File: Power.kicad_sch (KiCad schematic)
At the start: 10 parts

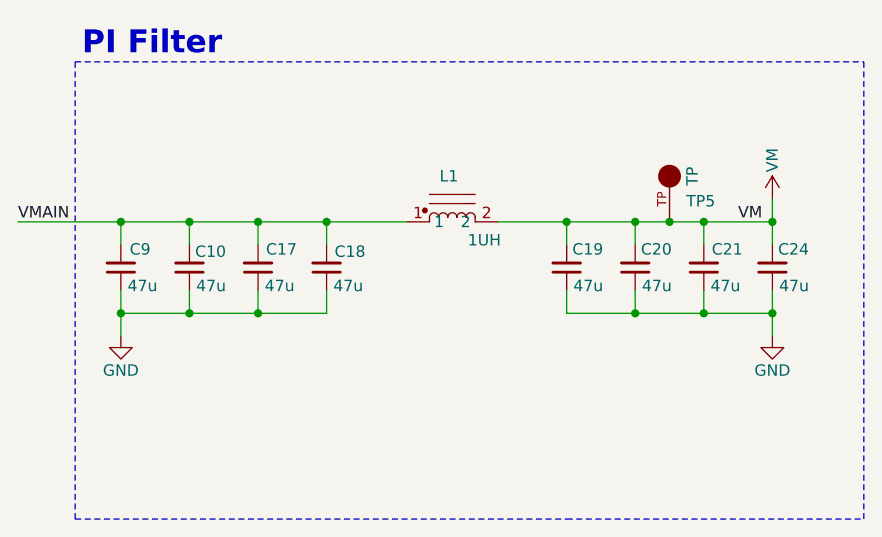
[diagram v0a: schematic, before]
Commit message: moved inductor and added leds
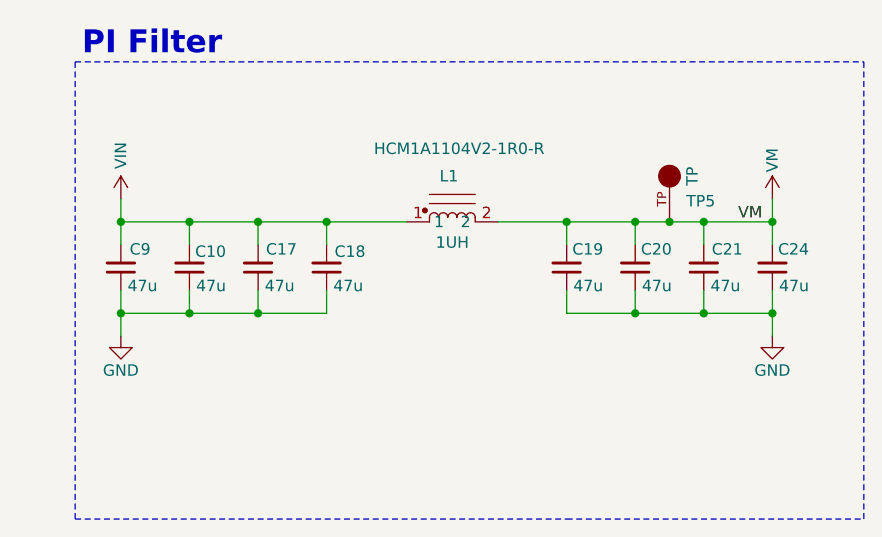
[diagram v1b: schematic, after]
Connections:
- net VMAIN renamed VIN
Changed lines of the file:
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@@
+	(wire
+		(pts
+			(xy 104.14 92.71) (xy 104.14 95.25)
+		)
+		(stroke
+			(width 0)
+			(type default)
+		)
+	)
 	(wire
 		(pts
@@
 		(pts
 			(xy 104.14 105.41) (xy 111.76 105.41)
-		)
-		(stroke
-			(width 0)
-			(type default)
-		)
-	)
-	(wire
-		(pts
-			(xy 92.71 95.25) (xy 104.14 95.25)
 		)
 		(stroke
@@
 	(label "VM"
 		(at 172.72 95.25 0)
-		(effects
-			(font
-				(size 1.27 1.27)
-			)
-			(justify left bottom)
-		)
-	)
-	(label "VMAIN"
-		(at 92.71 95.25 0)
 		(effects
 			(font
@@
 		(on_board yes)
 		(dnp no)
-		(fields_autoplaced yes)
 		(property "Reference" "L1"
 			(at 140.589 90.17 0)
@@
 		)
 		(property "Value" "1UH"
-			(at 144.526 97.282 0)
+			(at 140.97 97.536 0)
 			(do_not_autoplace yes)
 			(effects
@@
 		)
 		(property "Part" "HCM1A1104V2-1R0-R"
-			(at 146.558 99.568 0)
+			(at 141.732 87.122 0)
 			(do_not_autoplace yes)
 			(effects
@@
 					(size 1.27 1.27)
 				)
-				(hide yes)
 			)
 		)
@@
 					(unit 1)
 				)
+			)
+		)
+	)
+	(symbol
+		(lib_id "power:+3V3")
+		(at 104.14 92.71 0)
+		(unit 1)
+		(exclude_from_sim no)
+		(in_bom yes)
+		(on_board yes)
+		(dnp no)
+		(property "Reference" "#PWR01"
+			(at 104.14 96.52 0)
+			(effects
+				(font
+					(size 1.27 1.27)
+				)
+				(hide yes)
+			)
+		)
+		(property "Value" "VIN"
+			(at 104.14 87.884 90)
+			(effects
+				(font
+					(size 1.27 1.27)
+				)
+			)
+		)
+		(property "Footprint" ""
+			(at 104.14 92.71 0)
+			(effects
+				(font
+					(size 1.27 1.27)
+				)
+				(hide yes)
+			)
+		)
+		(property "Datasheet" ""
+			(at 104.14 92.71 0)
+			(effects
+				(font
+					(size 1.27 1.27)
+				)
+				(hide yes)
+			)
+		)
+		(property "Description" "Power symbol creates a global label with name \"+3V3\""
+			(at 104.14 92.71 0)
+			(effects
+				(font
+					(size 1.27 1.27)
+				)
+				(hide yes)
+			)
+		)
+		(pin "1"
+		)
+		(instances
+			(project "Avionics-RWboard"
+				(path "/833dc880-24c2-430b-8cf7-cc984eb87a9d/a3f3b3cb-ad78-4c13-ba45-eb5d7efe511d"
+					(reference "#PWR01")
+					(unit 1)
+				)
